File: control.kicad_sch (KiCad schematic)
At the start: 28 parts, among them J7 USB_C_Receptacle_USB2.0, J8 Conn_01x04_Male, J9 Conn_ARM_JTAG_SWD_10, U5 AMS1117-3.3, U6 STM32F042C4Tx

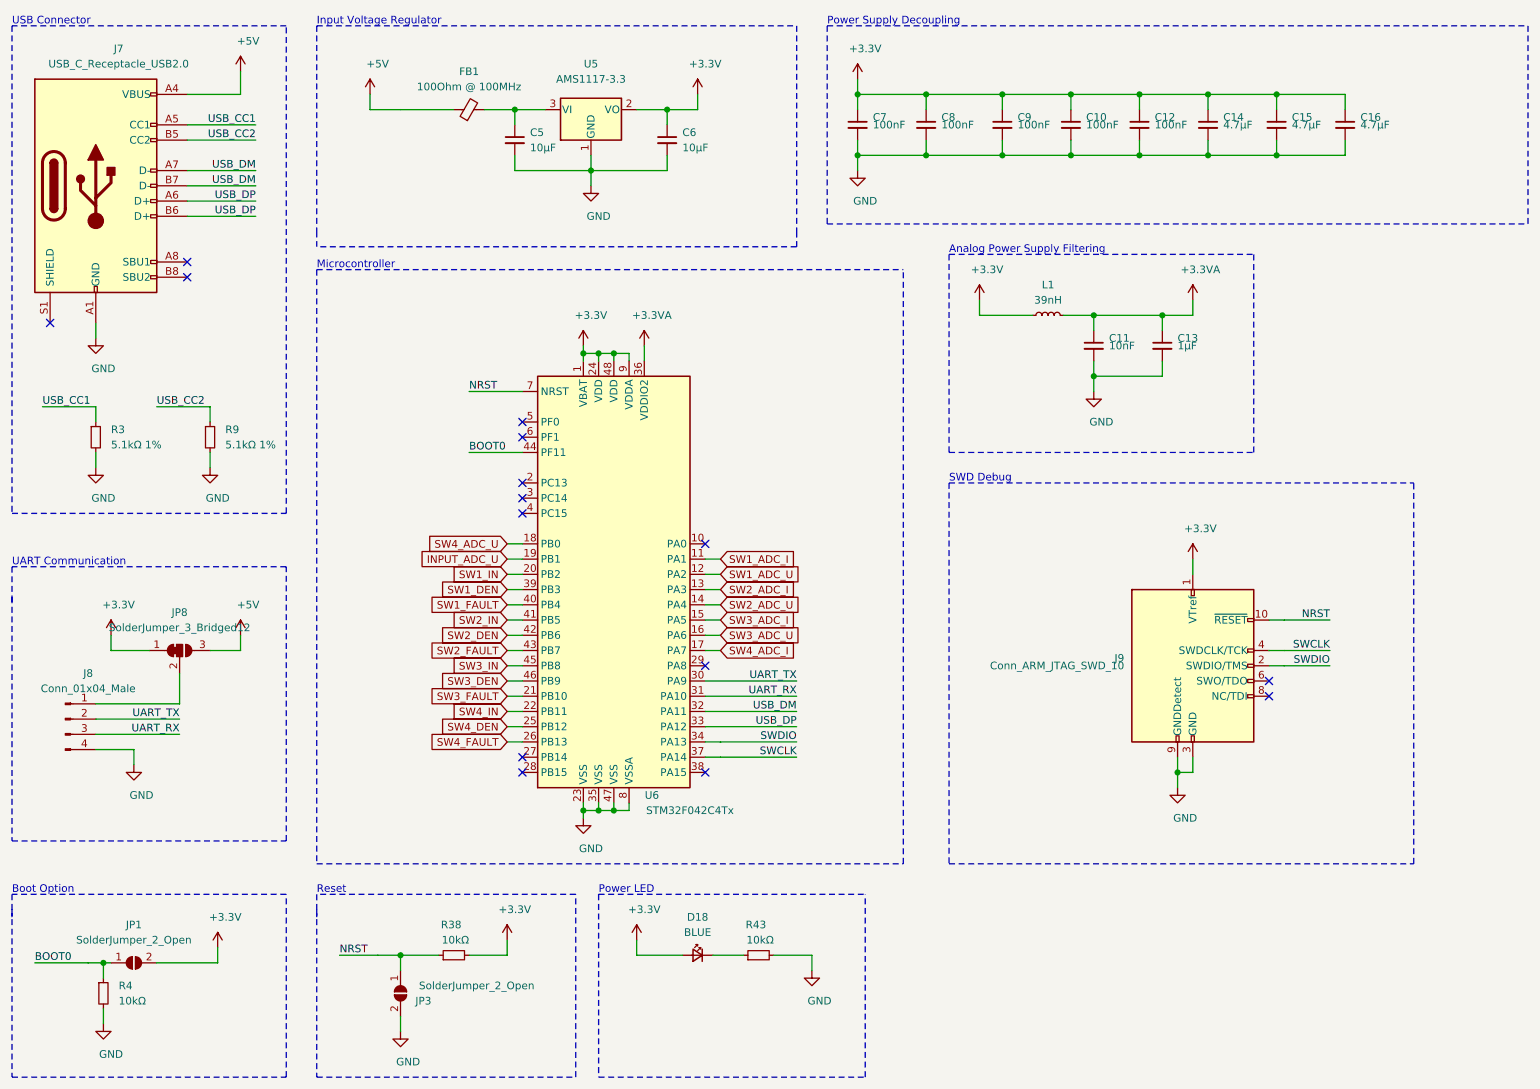
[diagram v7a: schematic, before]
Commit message: updated footprints, adjustments in placement
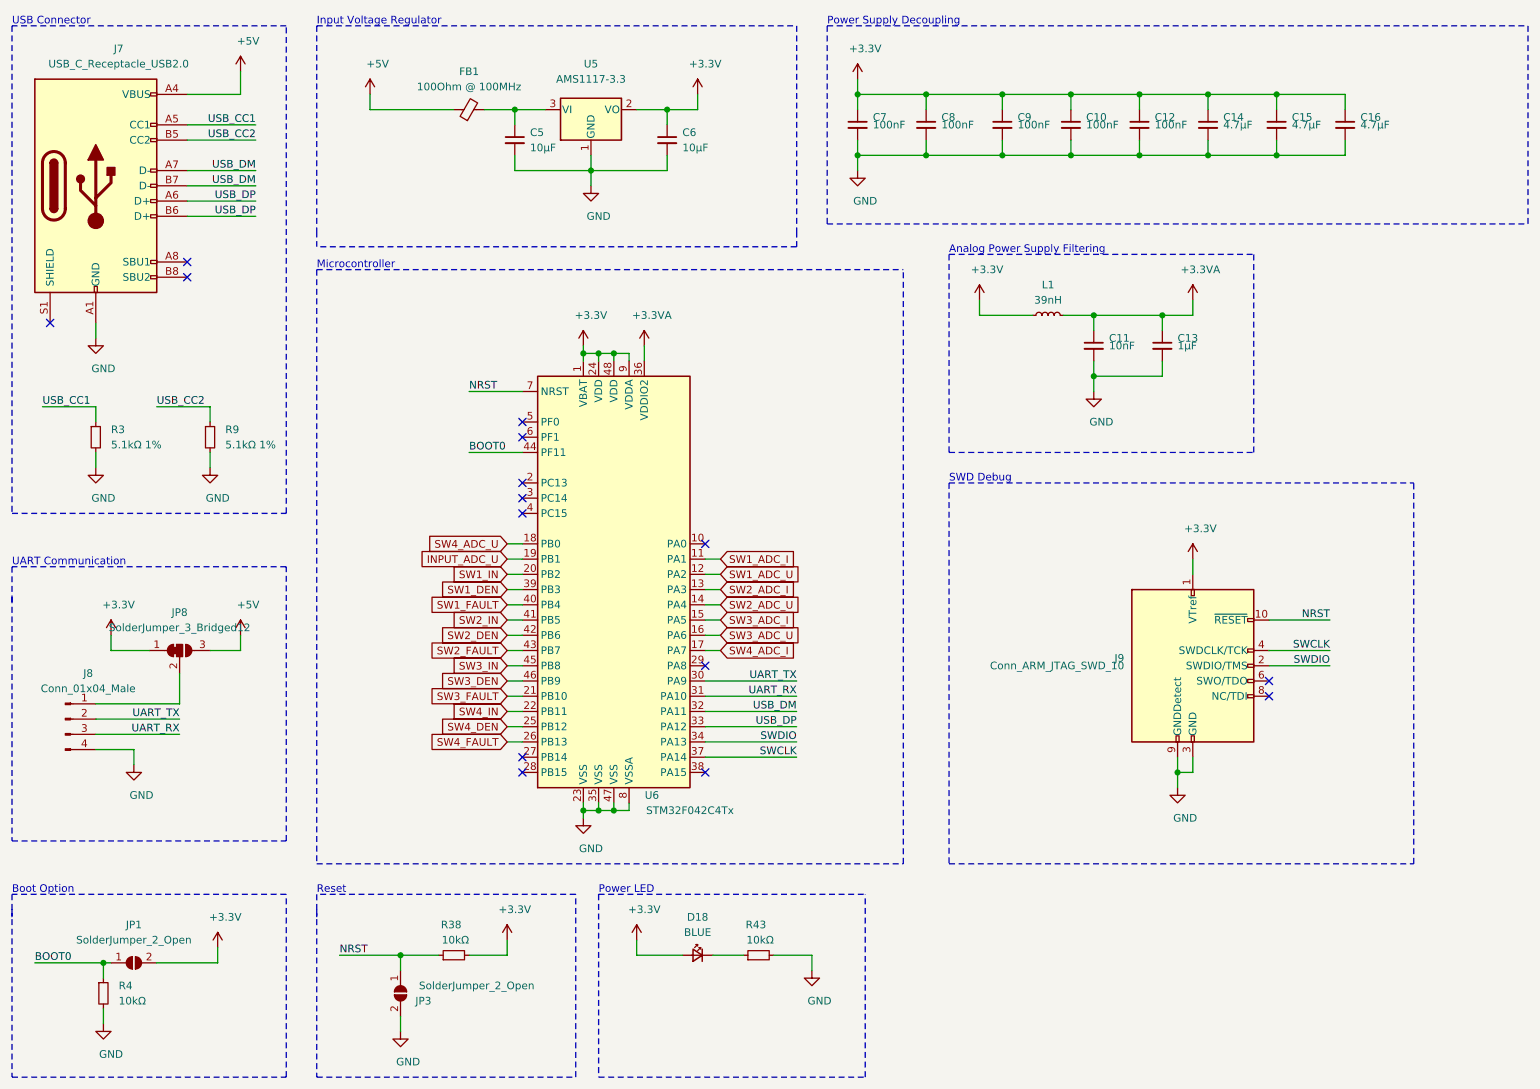
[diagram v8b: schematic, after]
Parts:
- J7: footprint Connector_USB:USB_C_Receptacle_Amphenol_12401610E4-2A -> Connector_USB:USB_C_Receptacle_HRO_TYPE-C-31-M-12
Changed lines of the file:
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@@
   (junction (at 228.6 39.37) (diameter 1.016) (color 0 0 0 0))
   (no_connect (at 46.99 59.69))
+  (no_connect (at 102.87 139.7))
+  (no_connect (at 133.35 142.24))
   (no_connect (at 24.13 67.31))
+  (no_connect (at 227.33 129.54))
+  (no_connect (at 102.87 96.52))
+  (no_connect (at 46.99 57.15))
+  (no_connect (at 102.87 99.06))
+  (no_connect (at 102.87 93.98))
+  (no_connect (at 102.87 86.36))
+  (no_connect (at 227.33 127))
+  (no_connect (at 133.35 104.14))
   (no_connect (at 102.87 83.82))
-  (no_connect (at 102.87 86.36))
-  (no_connect (at 102.87 96.52))
-  (no_connect (at 102.87 99.06))
-  (no_connect (at 102.87 139.7))
+  (no_connect (at 133.35 124.46))
   (no_connect (at 102.87 142.24))
-  (no_connect (at 133.35 104.14))
-  (no_connect (at 133.35 124.46))
-  (no_connect (at 133.35 142.24))
-  (no_connect (at 46.99 57.15))
-  (no_connect (at 102.87 93.98))
-  (no_connect (at 227.33 127))
-  (no_connect (at 227.33 129.54))
-  (wire (pts (xy 21.59 173.99) (xy 30.48 173.99))
+  (wire (pts (xy 21.59 173.99) (xy 33.02 173.99))
     (stroke (width 0) (type solid) (color 0 0 0 0))
   )
@@
     (stroke (width 0) (type solid) (color 0 0 0 0))
   )
-  (wire (pts (xy 30.48 173.99) (xy 33.02 173.99))
-    (stroke (width 0) (type solid) (color 0 0 0 0))
-  )
   (wire (pts (xy 31.75 67.31) (xy 31.75 69.85))
     (stroke (width 0) (type solid) (color 0 0 0 0))
@@
     (stroke (width 0) (type solid) (color 0 0 0 0))
   )
-  (wire (pts (xy 72.39 172.72) (xy 78.74 172.72))
+  (wire (pts (xy 72.39 172.72) (xy 82.55 172.72))
     (stroke (width 0) (type solid) (color 0 0 0 0))
   )
@@
     (stroke (width 0) (type solid) (color 0 0 0 0))
   )
-  (wire (pts (xy 78.74 172.72) (xy 82.55 172.72))
-    (stroke (width 0) (type solid) (color 0 0 0 0))
-  )
-  (wire (pts (xy 82.55 31.75) (xy 77.47 31.75))
-    (stroke (width 0) (type solid) (color 0 0 0 0))
-  )
-  (wire (pts (xy 82.55 31.75) (xy 91.44 31.75))
+  (wire (pts (xy 77.47 31.75) (xy 91.44 31.75))
     (stroke (width 0) (type solid) (color 0 0 0 0))
   )
@@
     (stroke (width 0) (type solid) (color 0 0 0 0))
   )
-  (wire (pts (xy 133.35 137.16) (xy 135.89 137.16))
-    (stroke (width 0) (type solid) (color 0 0 0 0))
-  )
-  (wire (pts (xy 133.35 139.7) (xy 135.89 139.7))
+  (wire (pts (xy 133.35 137.16) (xy 148.59 137.16))
+    (stroke (width 0) (type solid) (color 0 0 0 0))
+  )
+  (wire (pts (xy 133.35 139.7) (xy 148.59 139.7))
     (stroke (width 0) (type solid) (color 0 0 0 0))
   )
@@
     (stroke (width 0) (type solid) (color 0 0 0 0))
   )
-  (wire (pts (xy 135.89 137.16) (xy 148.59 137.16))
-    (stroke (width 0) (type solid) (color 0 0 0 0))
-  )
-  (wire (pts (xy 135.89 139.7) (xy 148.59 139.7))
-    (stroke (width 0) (type solid) (color 0 0 0 0))
-  )
   (wire (pts (xy 144.78 172.72) (xy 151.13 172.72))
     (stroke (width 0) (type solid) (color 0 0 0 0))
@@
     (stroke (width 0) (type solid) (color 0 0 0 0))
   )
-  (wire (pts (xy 227.33 116.84) (xy 229.87 116.84))
-    (stroke (width 0) (type solid) (color 0 0 0 0))
-  )
-  (wire (pts (xy 227.33 121.92) (xy 229.87 121.92))
-    (stroke (width 0) (type solid) (color 0 0 0 0))
-  )
-  (wire (pts (xy 227.33 124.46) (xy 229.87 124.46))
+  (wire (pts (xy 227.33 116.84) (xy 237.49 116.84))
+    (stroke (width 0) (type solid) (color 0 0 0 0))
+  )
+  (wire (pts (xy 227.33 121.92) (xy 237.49 121.92))
+    (stroke (width 0) (type solid) (color 0 0 0 0))
+  )
+  (wire (pts (xy 227.33 124.46) (xy 237.49 124.46))
     (stroke (width 0) (type solid) (color 0 0 0 0))
   )
@@
   )
   (wire (pts (xy 228.6 39.37) (xy 217.17 39.37))
-    (stroke (width 0) (type solid) (color 0 0 0 0))
-  )
-  (wire (pts (xy 229.87 116.84) (xy 237.49 116.84))
-    (stroke (width 0) (type solid) (color 0 0 0 0))
-  )
-  (wire (pts (xy 229.87 121.92) (xy 237.49 121.92))
-    (stroke (width 0) (type solid) (color 0 0 0 0))
-  )
-  (wire (pts (xy 229.87 124.46) (xy 237.49 124.46))
     (stroke (width 0) (type solid) (color 0 0 0 0))
   )
@@
     (property "Reference" "J7" (id 0) (at 35.56 21.59 0))
     (property "Value" "USB_C_Receptacle_USB2.0" (id 1) (at 35.56 24.13 0))
-    (property "Footprint" "Connector_USB:USB_C_Receptacle_Amphenol_12401610E4-2A" (id 2) (at 35.56 44.45 0)
-      (effects (font (size 1.27 1.27)) hide)
-    )
+    (property "Footprint" "Connector_USB:USB_C_Receptacle_HRO_TYPE-C-31-M-12" (id 2) (at 35.56 44.45 0)
+      (effects (font (size 1.27 1.27)) hide)
+    )
